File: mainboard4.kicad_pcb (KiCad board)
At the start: 4 copper layers, 100 x 100 mm, 241 parts, among them J1 Conn_01x04_Pin, J10 690-019-298-412, J12 USB3_A, J13 USB_C_Receptacle_USB2.0_16P, J14 Micro_SD_Card_Det, J16 USB_A_Stacked, J2 Conn_01x04_Pin, J3 Bus_M.2_Socket_B, J4 JST_SHBM04B-SRSS-TB, J5 THD-20-R, J6 Conn_02x07_Odd_Even, J7 Bus_M.2_Socket_E, J8 Barrel_Jack, J9 RJMG201K21120FR, SW1 Right angle Tact button, SW2 SW_DIP_x04, SW3 SW_Push, U1 74LVC1G07SE-7, U10 MCP2562-E-SN, U11 MCP2562-E-SN, U12 STM32H723VGT6, U13 LAN8742A, U14 JMS578, U15 CAT250xxx, U16 LAN9514, U19 CAT250xxx, U2 BNO086, U20 RT9742SNGV, U3 RT9742GGJ5, U4 ASEK-32.768KHZ-L-R-T, U5 AP64502QSP-13, U6 ASEK-32.768KHZ-L-R-T, U7 AP64502, U8 AP22653W6, U9 CH221K, Y1 32.768khz, Y2 16Mhz, Y3 25Mhz, Y4 30Mhz, Y6 25Mhz

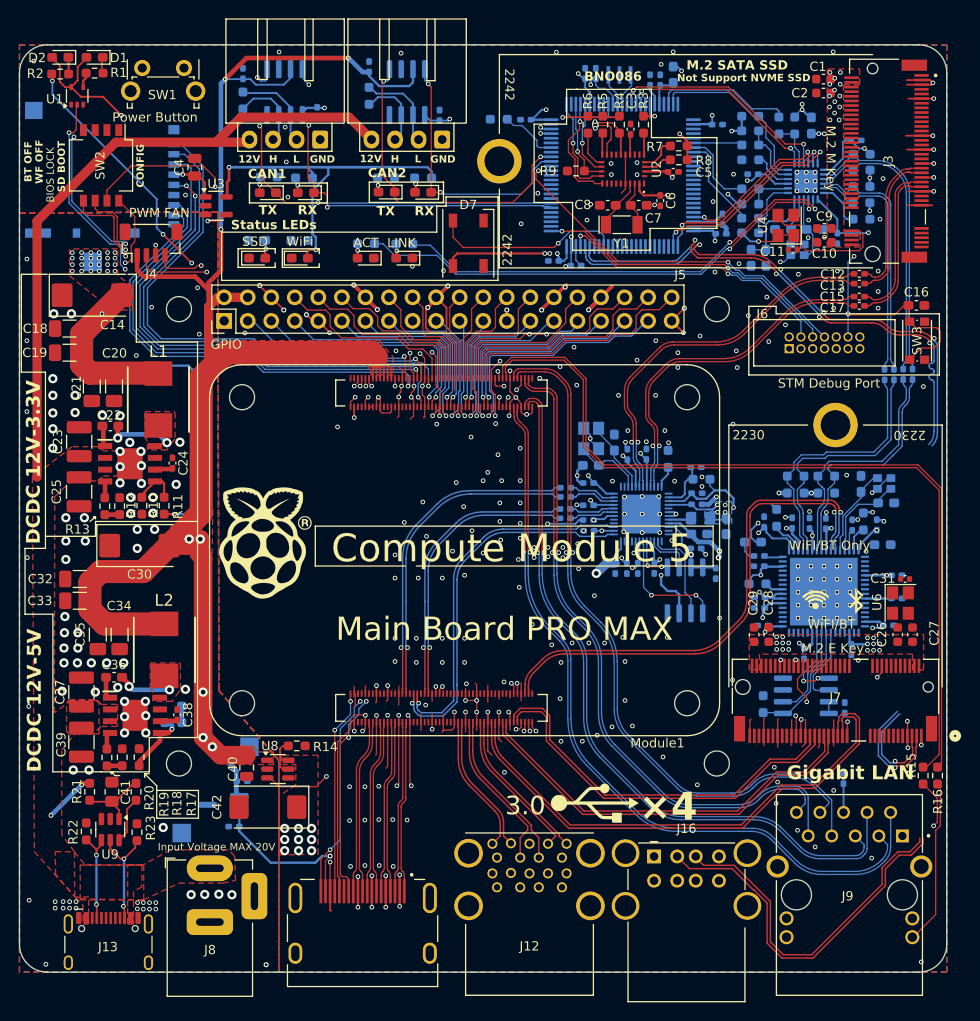
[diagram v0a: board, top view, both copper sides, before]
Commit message: add pcie line
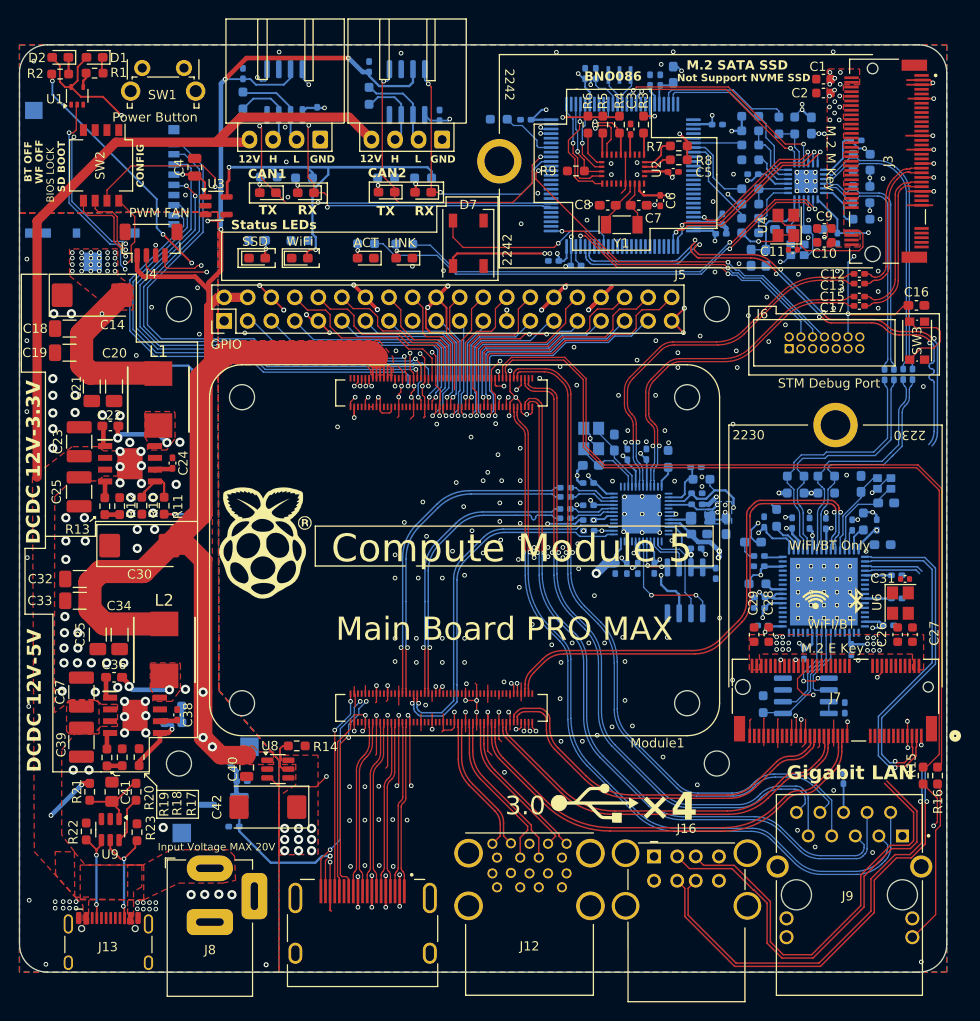
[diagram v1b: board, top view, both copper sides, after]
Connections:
- J7 pad 35: /CM5_HighSpeed/PCIE_TX_P -> /CM5_HighSpeed/PCIE_TX_N
- J7 pad 37: /CM5_HighSpeed/PCIE_TX_N -> /CM5_HighSpeed/PCIE_TX_P
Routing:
- net /USB2Ethernet/USB4DN: track 0.00 -> 48.2 mm, vias 0 -> 1
- net /USB2Ethernet/USB4DP: track 0.00 -> 47.3 mm, vias 0 -> 1
- net /CM5_PCIe/USB_D-: track 11.5 -> 36.9 mm
- net /CM5_PCIe/USB_D+: track 12.9 -> 37.5 mm
- net /CM5_HighSpeed/PCIE_TX_N: track 56.9 -> 49.1 mm
- net /USB2Ethernet/USB5DN: track 40.3 -> 48.0 mm
- net /USB2Ethernet/USB5DP: track 37.7 -> 45.0 mm
- net /CM5_HighSpeed/PCIE_TX_P: track 54.5 -> 47.9 mm
- net /MCU/USB_DN: track 56.8 -> 63.2 mm
- net /MCU/USB_DP: track 56.4 -> 62.5 mm
- net +5V: track 211.5 -> 208.0 mm, vias 8 -> 6
- net /CM5_HighSpeed/PCIE_CLK_P: track 43.2 -> 40.7 mm
- net /CM5_HighSpeed/PCIE_CLK_N: track 43.2 -> 40.7 mm
- net /VBUS: track 88.7 -> 90.6 mm
- net /CM5_HighSpeed/PCIE_nRST: track 40.9 -> 42.0 mm
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
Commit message: add usb2.0 line
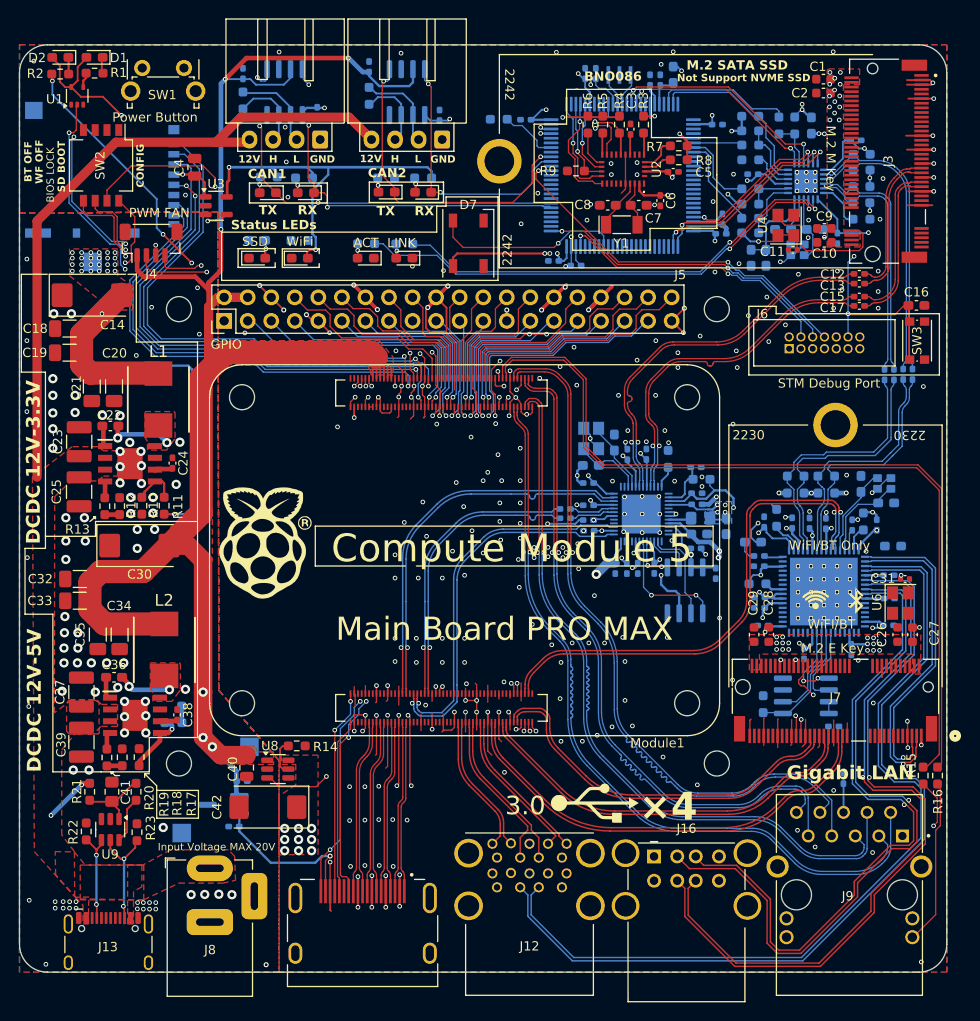
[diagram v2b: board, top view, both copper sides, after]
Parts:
- removed C107, C108: 0.1uF, Capacitor_SMD:C_0402_1005Metric_Pad0.74x0.62mm_HandSolder
- moved C134 2.33 mm to (195.8, 108.5), turned to 0 degrees
- moved FB5 1.13 mm to (202.2, 89.0)
- moved C112 0.85 mm to (201.8, 92.2)
- moved C121 0.80 mm to (201.8, 94.7)
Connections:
- J12 pad A2: unconnected-(J12-D--PadA2) -> /USB2DN
- J12 pad A3: unconnected-(J12-D+-PadA3) -> /USB2DP
- U14 pad 22: /USB2SATA/SS_RX_N -> /CM5_HighSpeed/USB3-1-TX_N
- U14 pad 23: /USB2SATA/SS_RX_P -> /CM5_HighSpeed/USB3-1-TX_P
- U16 pad 3: /MCU/USB_DN -> /USB2DN
- U16 pad 4: /MCU/USB_DP -> /USB2DP
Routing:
- net /USB2DN: track 0.00 -> 94.6 mm
- net /USB2DP: track 0.00 -> 92.8 mm
- net /MCU/USB_DN: track 63.2 -> 0.00 mm, vias 4 -> 0
- net /MCU/USB_DP: track 62.5 -> 0.00 mm, vias 4 -> 0
- net /USB2Ethernet/USB4DN: track 48.2 -> 79.5 mm
- net /USB2Ethernet/USB4DP: track 47.3 -> 77.7 mm
- net /USB2Ethernet/USB5DN: track 48.0 -> 77.3 mm, vias 0 -> 1
- net /USB2Ethernet/USB5DP: track 45.0 -> 74.0 mm, vias 0 -> 1
- net /CM5_HighSpeed/USB3-1-TX_N: track 35.1 -> 41.6 mm
- net /CM5_HighSpeed/USB3-1-TX_P: track 35.7 -> 41.7 mm
- net /USB2SATA/SS_RX_P: track 5.12 -> 0.00 mm
- net /USB2SATA/SS_RX_N: track 5.10 -> 0.00 mm
- net NRST: track 68.5 -> 63.7 mm
- net /CM5_GPIO/TRD2_N: track 73.8 -> 76.9 mm
- net /CM5_PCIe/USB_D-: track 36.9 -> 34.8 mm
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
